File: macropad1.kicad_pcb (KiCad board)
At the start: 2 copper layers, 139.7 x 69.8 mm, 62 parts, among them J1 Conn_01x04, J2 USB_B_Mini, J3 AVR-ISP-6, P1 TestPoint, P12 TestPoint, P20 TestPoint, P21 TestPoint, P22 TestPoint, P28 TestPoint, P29 TestPoint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

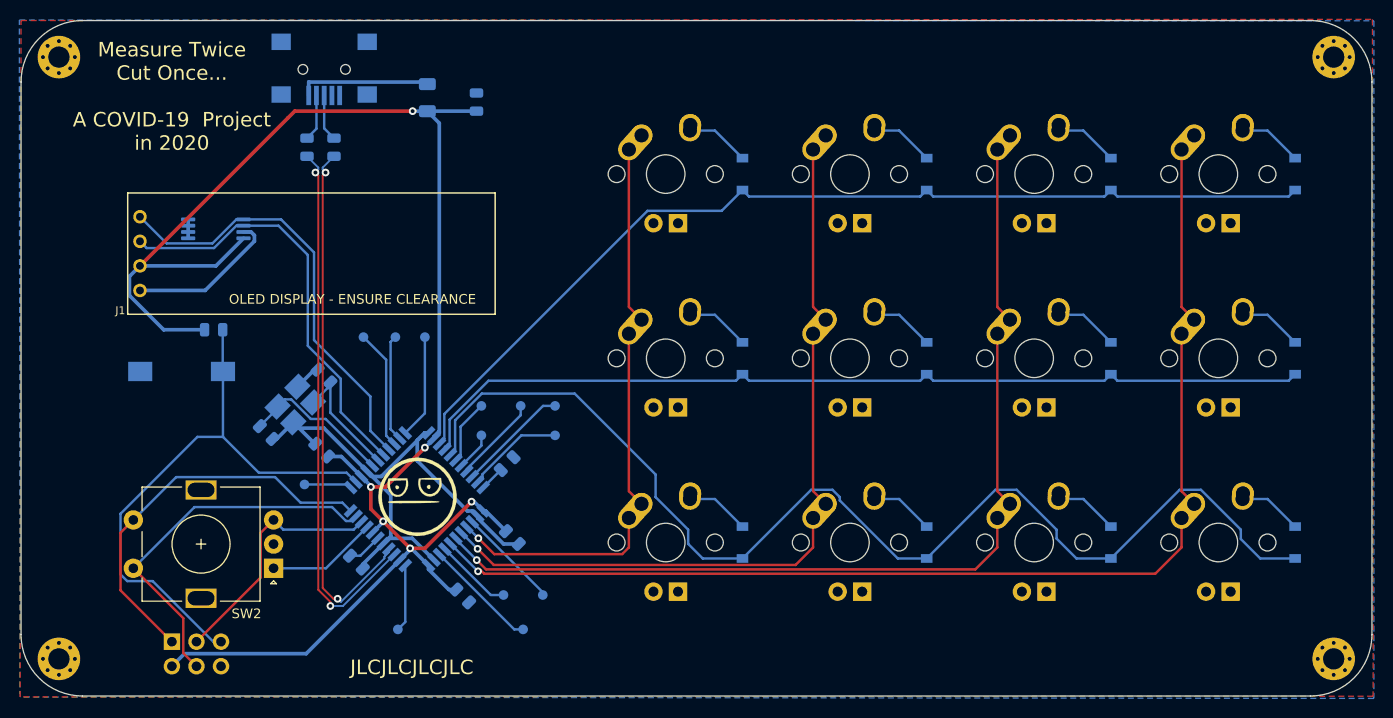
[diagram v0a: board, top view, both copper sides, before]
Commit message: Adds single color backlighting to each key :)
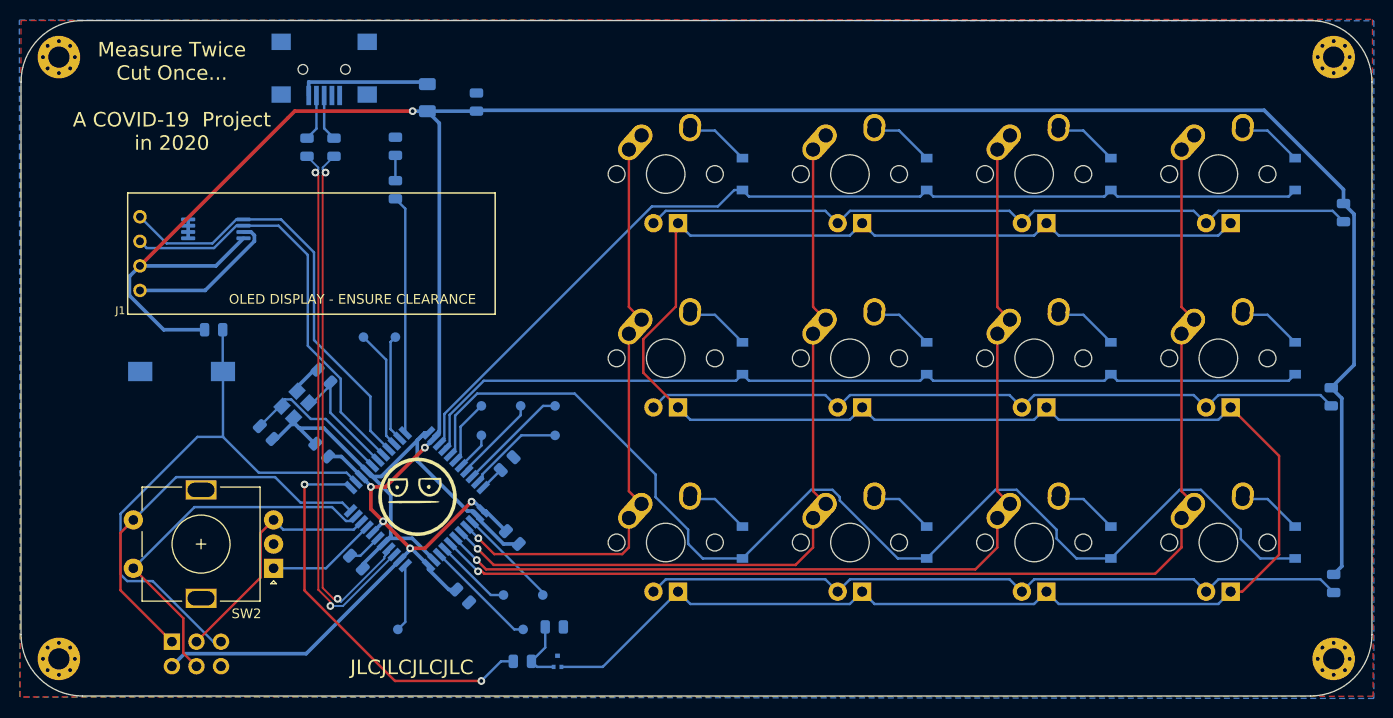
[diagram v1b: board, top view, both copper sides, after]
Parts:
- removed P12, P22: TestPoint, TestPoint:TestPoint_Pad_D1.0mm
- added D13: LED, LED_SMD:LED_0805_2012Metric, B.Cu at (72.4, 33.4)
- added Q1: Q_NMOS_DGS, Package_TO_SOT_SMD:SOT-723, B.Cu at (89.2, 86.6)
- added R10: 330, Resistor_SMD:R_0805_2012Metric, B.Cu at (169.4, 78.6)
- added R5: 330, Resistor_SMD:R_0805_2012Metric, B.Cu at (72.4, 37.8)
- added R6: 470, Resistor_SMD:R_0805_2012Metric, B.Cu at (85.5, 86.6)
- added R7: 10k, Resistor_SMD:R_0805_2012Metric, B.Cu at (88.8, 83.1)
- added R8: 330, Resistor_SMD:R_0805_2012Metric, B.Cu at (170.4, 40.2)
- added R9: 330, Resistor_SMD:R_0805_2012Metric, B.Cu at (169.2, 59.3)
- J3: footprint artwork:ISP-6 -> Connector_PinHeader_2.54mm:PinHeader_2x03_P2.54mm_Vertical
- Y1: footprint Crystal:Crystal_SMD_3225-4Pin_3.2x2.5mm_HandSoldering -> Crystal:Crystal_SMD_3225-4Pin_3.2x2.5mm
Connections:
- MX10 pad 4: Net-(MX10-Pad4) -> Net-(MX1-Pad4)
- MX11 pad 3: Net-(MX11-Pad3) -> Net-(MX10-Pad3)
- MX11 pad 4: Net-(MX11-Pad4) -> Net-(MX1-Pad4)
- MX12 pad 3: Net-(MX12-Pad3) -> Net-(MX10-Pad3)
- MX12 pad 4: Net-(MX12-Pad4) -> Net-(MX1-Pad4)
- MX2 pad 3: Net-(MX2-Pad3) -> Net-(MX1-Pad3)
- MX2 pad 4: Net-(MX2-Pad4) -> Net-(MX1-Pad4)
- MX3 pad 3: Net-(MX3-Pad3) -> Net-(MX1-Pad3)
- MX3 pad 4: Net-(MX3-Pad4) -> Net-(MX1-Pad4)
- MX4 pad 3: Net-(MX4-Pad3) -> Net-(MX1-Pad3)
- MX4 pad 4: Net-(MX4-Pad4) -> Net-(MX1-Pad4)
- MX5 pad 4: Net-(MX5-Pad4) -> Net-(MX1-Pad4)
- MX6 pad 3: Net-(MX6-Pad3) -> Net-(MX5-Pad3)
- MX6 pad 4: Net-(MX6-Pad4) -> Net-(MX1-Pad4)
- MX7 pad 3: Net-(MX7-Pad3) -> Net-(MX5-Pad3)
- MX7 pad 4: Net-(MX7-Pad4) -> Net-(MX1-Pad4)
- MX8 pad 3: Net-(MX8-Pad3) -> Net-(MX5-Pad3)
- MX8 pad 4: Net-(MX8-Pad4) -> Net-(MX1-Pad4)
- MX9 pad 3: Net-(MX9-Pad3) -> Net-(MX10-Pad3)
- MX9 pad 4: Net-(MX9-Pad4) -> Net-(MX1-Pad4)
- U1 pad 12: Net-(P12-Pad1) -> /PWM1
- U1 pad 22: Net-(P22-Pad1) -> /status_led
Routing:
- net Net-(MX1-Pad4): track 0.00 -> 242.2 mm
- net +5V: track 175.7 -> 311.2 mm
- net Net-(MX1-Pad3): track 0.00 -> 75.5 mm
- net Net-(MX10-Pad3): track 0.00 -> 74.6 mm
- net Net-(MX5-Pad3): track 0.00 -> 74.3 mm
- net /PWM1: track 0.00 -> 42.2 mm, vias 0 -> 2
- net /status_led: track 0.00 -> 24.6 mm
- net Net-(P22-Pad1): track 10.7 -> 0.00 mm
- net Net-(Q1-Pad2): track 0.00 -> 6.68 mm
- net Net-(P12-Pad1): track 4.89 -> 0.00 mm
- net Net-(D13-Pad2): track 0.00 -> 2.62 mm
